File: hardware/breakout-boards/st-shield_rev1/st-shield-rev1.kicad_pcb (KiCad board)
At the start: 4 copper layers, 63.5 x 50.8 mm, 187 parts, among them P1 CONN_01X06, P10 TST, P11 TST, P12 TST, P13 TST, P14 TST, P15 TST, P16 TST, P17 TST, P18 TST, P19 TST, P2 CONN_02X20, P20 TST, P21 TST, P22 TST, P23 TST, P24 TST, P25 TST, P26 TST, P27 TST, P28 TST, P3 CH_A, P4 CH_B, P5 CH_C, P6 PVDD, P7 GND, P8 TST, P9 TST, Q1 Q_PMOS_GSD, Q2 Q_PMOS_GSD, Q3 Q_NMOS_DGS, Q4 Q_NMOS_DGS, Q5 Q_NMOS_DGS, Q6 Q_NMOS_DGS, Q7 Q_NMOS_DGS, Q8 Q_NMOS_DGS, U1 DRV8301_DCA_56, U2 AD8691, U3 AD8691, U4 AD8691, U5 MCP9700-X_TT, U6 MCP9700-X_TT, U7 TLV62565DBVR, U8 AD8691

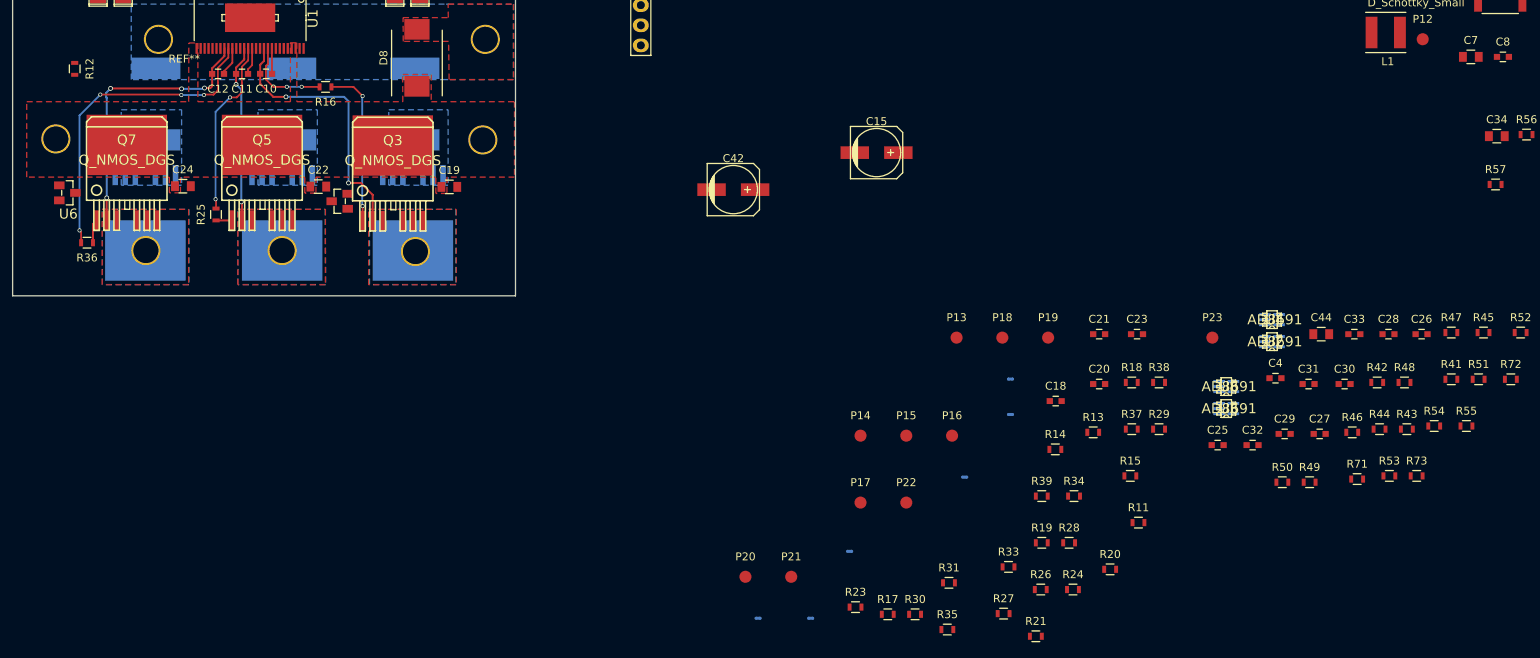
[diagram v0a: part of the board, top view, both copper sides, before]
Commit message: st-shield: more board work. maybe remove some op amps?
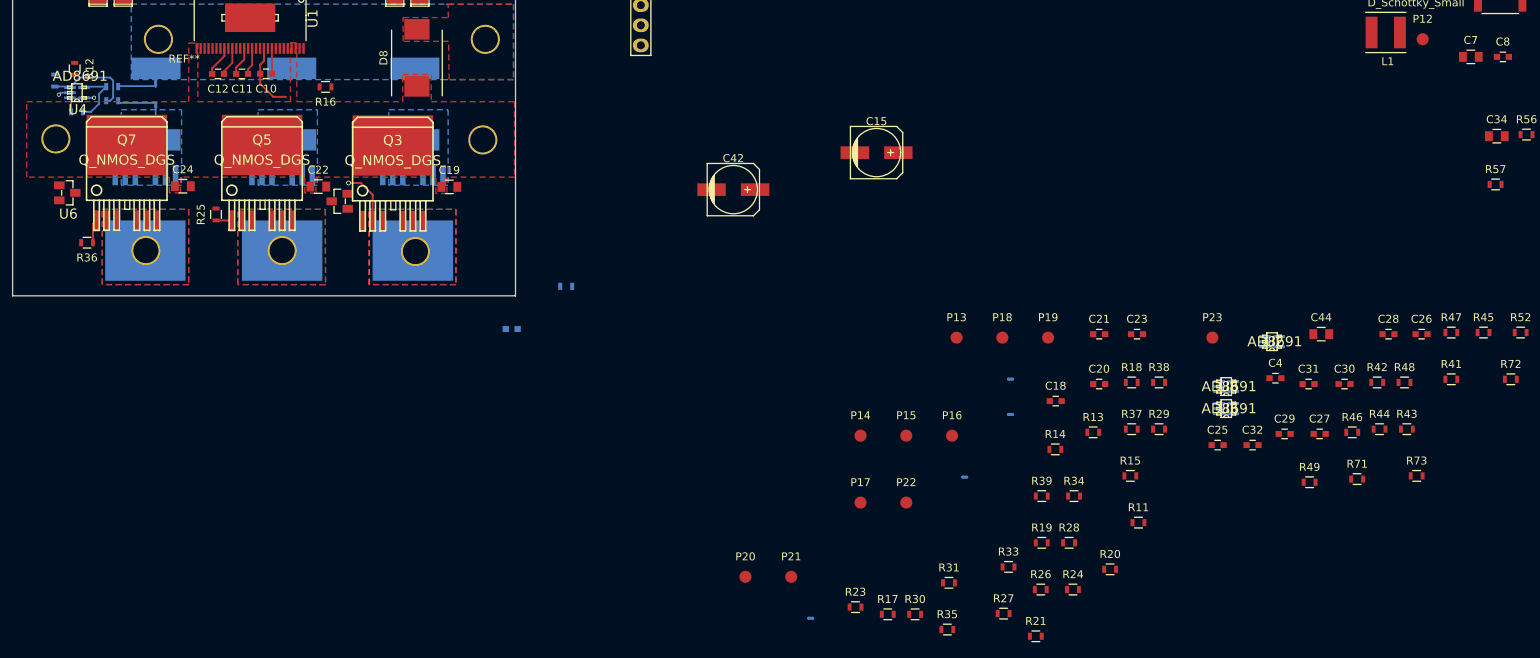
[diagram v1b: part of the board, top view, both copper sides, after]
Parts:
- C33, R50, R51, R53, R54, R55: moved to B.Cu
- moved R51 176.5 mm to (132.0, 95.5)
- moved R54 175.9 mm to (127.5, 98.7)
- moved R53 175.7 mm to (124.7, 94.7), turned to 90 degrees
- moved R50 155.4 mm to (132.0, 97.3)
- moved U4 153.6 mm to (127.5, 96.3)
- moved R55 115.0 mm to (189.3, 120.7), turned to 180 degrees
- moved C33 106.4 mm to (182.4, 126.1)
- moved W5 104.2 mm to (137.5, 97.8), turned to 90 degrees
- moved W6 101.7 mm to (137.4, 95.2), turned to 270 degrees
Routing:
- net /MOSFET Array/C_HI: track 40.8 -> 0.00 mm, vias 4 -> 0
- net /MOSFET Array/MOTOR_C: track 35.3 -> 3.86 mm, vias 4 -> 0
- net /MOSFET Array/B_HI: track 22.4 -> 0.00 mm, vias 2 -> 0
- net Net-(P13-Pad1): track 20.2 -> 0.00 mm, vias 2 -> 0
- net /MOSFET Array/MOTOR_B: track 22.4 -> 3.64 mm, vias 2 -> 0
- net /MOSFET Array/MOTOR_A: track 34.2 -> 15.7 mm, vias 2 -> 1
- net Net-(R50-Pad1): track 0.00 -> 11.3 mm
- net /MOSFET Array/A_HI: track 11.4 -> 0.19 mm, vias 2 -> 0
- net Net-(R51-Pad1): track 0.00 -> 7.85 mm
- net /MOSFET Array/CUR_CP: track 0.00 -> 4.86 mm
- net /MOSFET Array/CUR_CN: track 0.00 -> 4.76 mm
- net /FET Driver/SL_C: track 0.00 -> 4.18 mm
- net GND: track 0.00 -> 3.61 mm, vias 0 -> 1
- net Net-(R54-Pad1): track 0.00 -> 1.82 mm
- net 3V3: track 0.00 -> 1.27 mm, vias 0 -> 1
- added copper zone on In1.Cu, net 3V3
- added copper zone on In2.Cu, net GND
